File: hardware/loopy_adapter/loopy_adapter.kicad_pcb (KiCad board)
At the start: 2 copper layers, 96.6 x 25.5 mm, 3 parts, among them J1 CART SLOT TOP ROW, J2 CART SLOT BOTTOM ROW, J3 Loopy_Slot

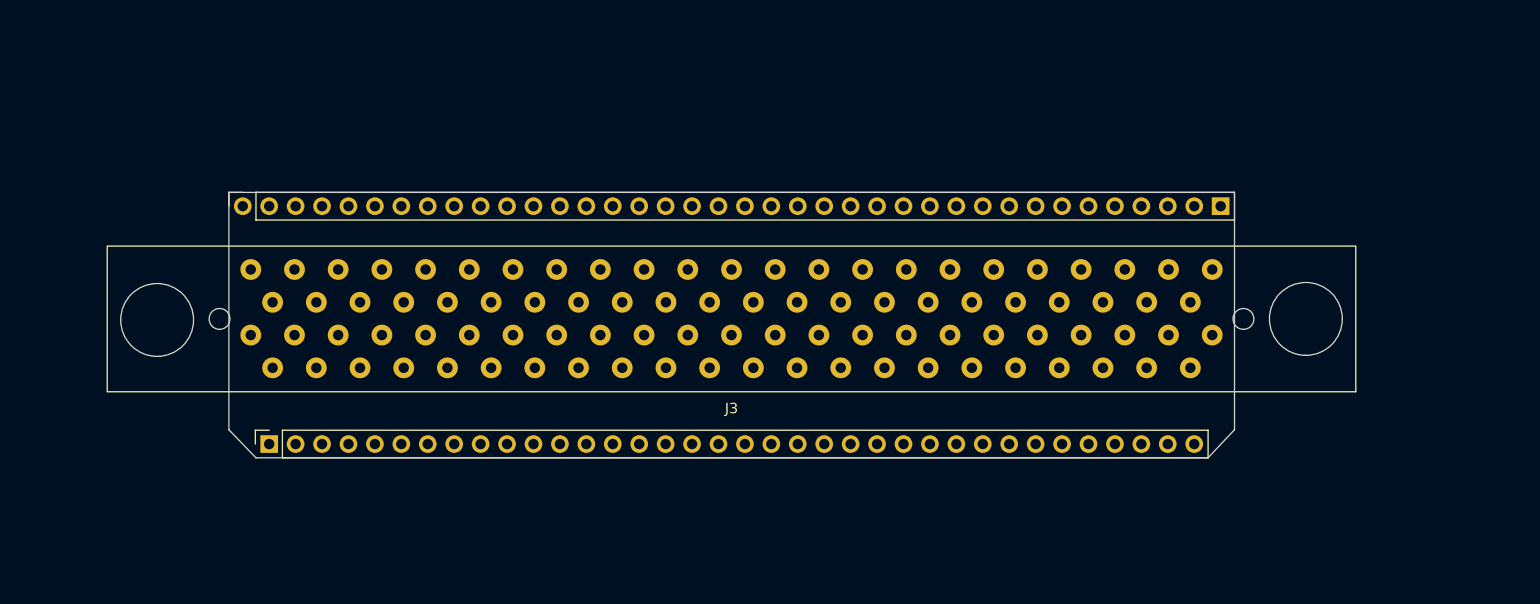
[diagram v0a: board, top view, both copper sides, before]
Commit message: Loopy adapter wired
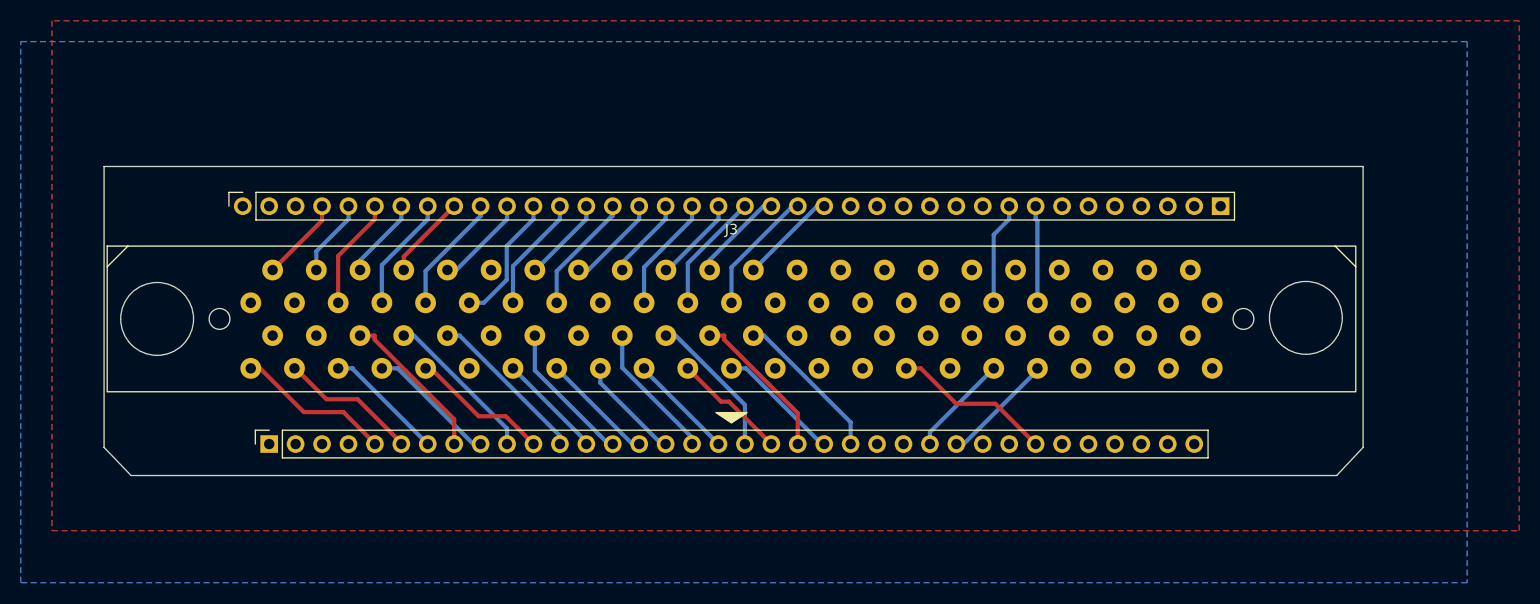
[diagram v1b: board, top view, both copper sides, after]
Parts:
- turned J3 to 0 degrees
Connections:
- J3 pad 1: unconnected-(J3-+5V-Pad1) -> +5V
- J3 pad 11: unconnected-(J3-~{RAMWE}-Pad11) -> D6
- J3 pad 13: unconnected-(J3-GND-Pad13) -> GND
- J3 pad 14: unconnected-(J3-+5V-Pad14) -> +5V
- J3 pad 22: unconnected-(J3-A12-Pad22) -> D34
- J3 pad 23: unconnected-(J3-A10-Pad23) -> D35
- J3 pad 24: unconnected-(J3-A8-Pad24) -> D36
- J3 pad 25: unconnected-(J3-A6-Pad25) -> D37
- J3 pad 26: unconnected-(J3-A13-Pad26) -> A15
- J3 pad 27: unconnected-(J3-A15-Pad27) -> A14
- J3 pad 28: unconnected-(J3-A20-Pad28) -> A13
- J3 pad 29: unconnected-(J3-+5V-Pad29) -> +5V
- J3 pad 30: unconnected-(J3-A3-Pad30) -> A12
- J3 pad 31: unconnected-(J3-A21-Pad31) -> A11
- J3 pad 32: unconnected-(J3-A1-Pad32) -> A10
- J3 pad 33: unconnected-(J3-A0-Pad33) -> A9
- J3 pad 35: unconnected-(J3-D0-Pad35) -> A8
- J3 pad 36: unconnected-(J3-~{RESET}-Pad36) -> A7
- J3 pad 37: unconnected-(J3-D2-Pad37) -> A6
- J3 pad 38: unconnected-(J3-D3-Pad38) -> A5
- J3 pad 39: unconnected-(J3-D14-Pad39) -> A4
- J3 pad 40: unconnected-(J3-D4-Pad40) -> A3
- J3 pad 41: unconnected-(J3-D6-Pad41) -> A2
- J3 pad 42: unconnected-(J3-D8-Pad42) -> A1
- J3 pad 44: unconnected-(J3-D10-Pad44) -> A0
- J3 pad 45: unconnected-(J3-GND-Pad45) -> GND
- J3 pad 47: unconnected-(J3-GND-Pad47) -> GND
- J3 pad 54: unconnected-(J3-~{CS6}-Pad54) -> D42
- J3 pad 56: unconnected-(J3-~{OE}-Pad56) -> D43
- J3 pad 57: unconnected-(J3-+5V-Pad57) -> +5V
- J3 pad 60: unconnected-(J3-CLK-Pad60) -> CLK2
- J3 pad 67: unconnected-(J3-A11-Pad67) -> D46
- J3 pad 68: unconnected-(J3-A9-Pad68) -> D47
- J3 pad 69: unconnected-(J3-A7-Pad69) -> D48
- J3 pad 70: unconnected-(J3-A5-Pad70) -> D49
- J3 pad 71: unconnected-(J3-A14-Pad71) -> D29
- J3 pad 72: unconnected-(J3-A17-Pad72) -> D28
- J3 pad 73: unconnected-(J3-A16-Pad73) -> D27
- J3 pad 74: unconnected-(J3-A18-Pad74) -> D26
- J3 pad 75: unconnected-(J3-GND-Pad75) -> GND
- J3 pad 76: unconnected-(J3-A19-Pad76) -> D25
- J3 pad 77: unconnected-(J3-A4-Pad77) -> D24
- J3 pad 78: unconnected-(J3-A2-Pad78) -> D23
- J3 pad 81: unconnected-(J3-D1-Pad81) -> D22
- J3 pad 82: unconnected-(J3-D12-Pad82) -> D14
- J3 pad 83: unconnected-(J3-D13-Pad83) -> D15
- J3 pad 84: unconnected-(J3-D15-Pad84) -> D4
- J3 pad 85: unconnected-(J3-D5-Pad85) -> D40
- J3 pad 86: unconnected-(J3-D7-Pad86) -> D41
- J3 pad 88: unconnected-(J3-D9-Pad88) -> D3
- J3 pad 89: unconnected-(J3-+5V-Pad89) -> +5V
- J3 pad 9: unconnected-(J3-~{CS2}-Pad9) -> D7
- J3 pad 90: unconnected-(J3-D11-Pad90) -> D2
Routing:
- net D22: track 0.00 -> 15.6 mm
- net CLK2: track 0.00 -> 15.4 mm
- net D15: track 0.00 -> 15.1 mm
- net D2: track 0.00 -> 15.0 mm
- net D40: track 0.00 -> 15.0 mm
- net D46: track 0.00 -> 14.9 mm
- net D48: track 0.00 -> 14.8 mm
- net D29: track 0.00 -> 14.1 mm
- net D24: track 0.00 -> 13.8 mm
- net D14: track 0.00 -> 13.4 mm
- net D3: track 0.00 -> 13.3 mm
- net D27: track 0.00 -> 13.2 mm
- net A8: track 0.00 -> 12.7 mm
- net D4: track 0.00 -> 12.5 mm
- net D35: track 0.00 -> 12.2 mm
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- added copper zone on F.Cu, net +5V
- added copper zone on B.Cu, net GND
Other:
- board size 96.6 x 25.5 mm -> 121 x 29.7 mm
